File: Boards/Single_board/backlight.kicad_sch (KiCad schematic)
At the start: 38 parts

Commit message: some progress on the arduino boilerplate
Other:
- company: (none) -> Pablo Ortiz López, Evan MacDonald
- title: (none) -> Backlight for DSKY Keyboard
- moved on the sheet: D1, D10, D11, D12, D13, D14, D15, D16, D17, D18, D19, D2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

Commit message: Visual Schematic improvements
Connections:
- net PWMcom renamed PWMCom
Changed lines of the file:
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@@
 		)
 	)
-	(global_label "PWMcom"
-		(shape input)
+	(hierarchical_label "PWMCom"
+		(shape output)
 		(at 144.78 120.65 270)
 		(fields_autoplaced yes)
@@
 			(justify right)
 		)
-		(property "Intersheetrefs" "${INTERSHEET_REFS}"
-			(at 144.78 131.7389 90)
-			(effects
-				(font
-					(size 1.27 1.27)
-				)
-				(justify right)
-				(hide yes)
-			)
-		)
 	)

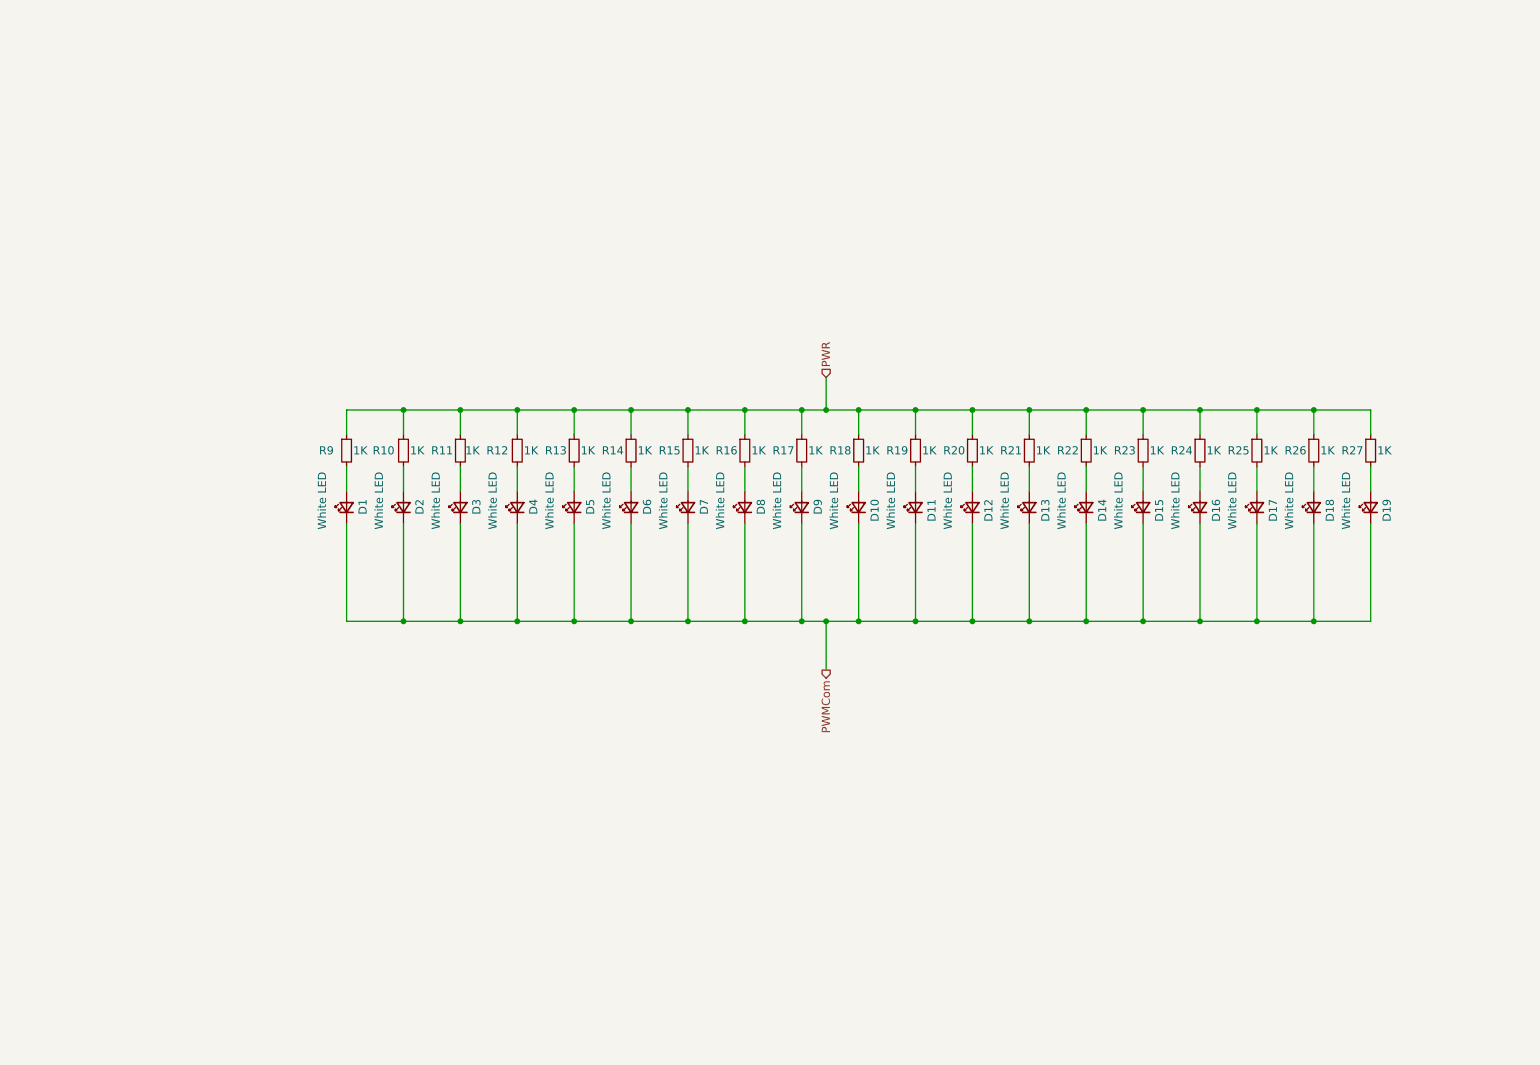
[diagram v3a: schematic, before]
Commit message: Start RGB LED + hotswap socket redesign of single board
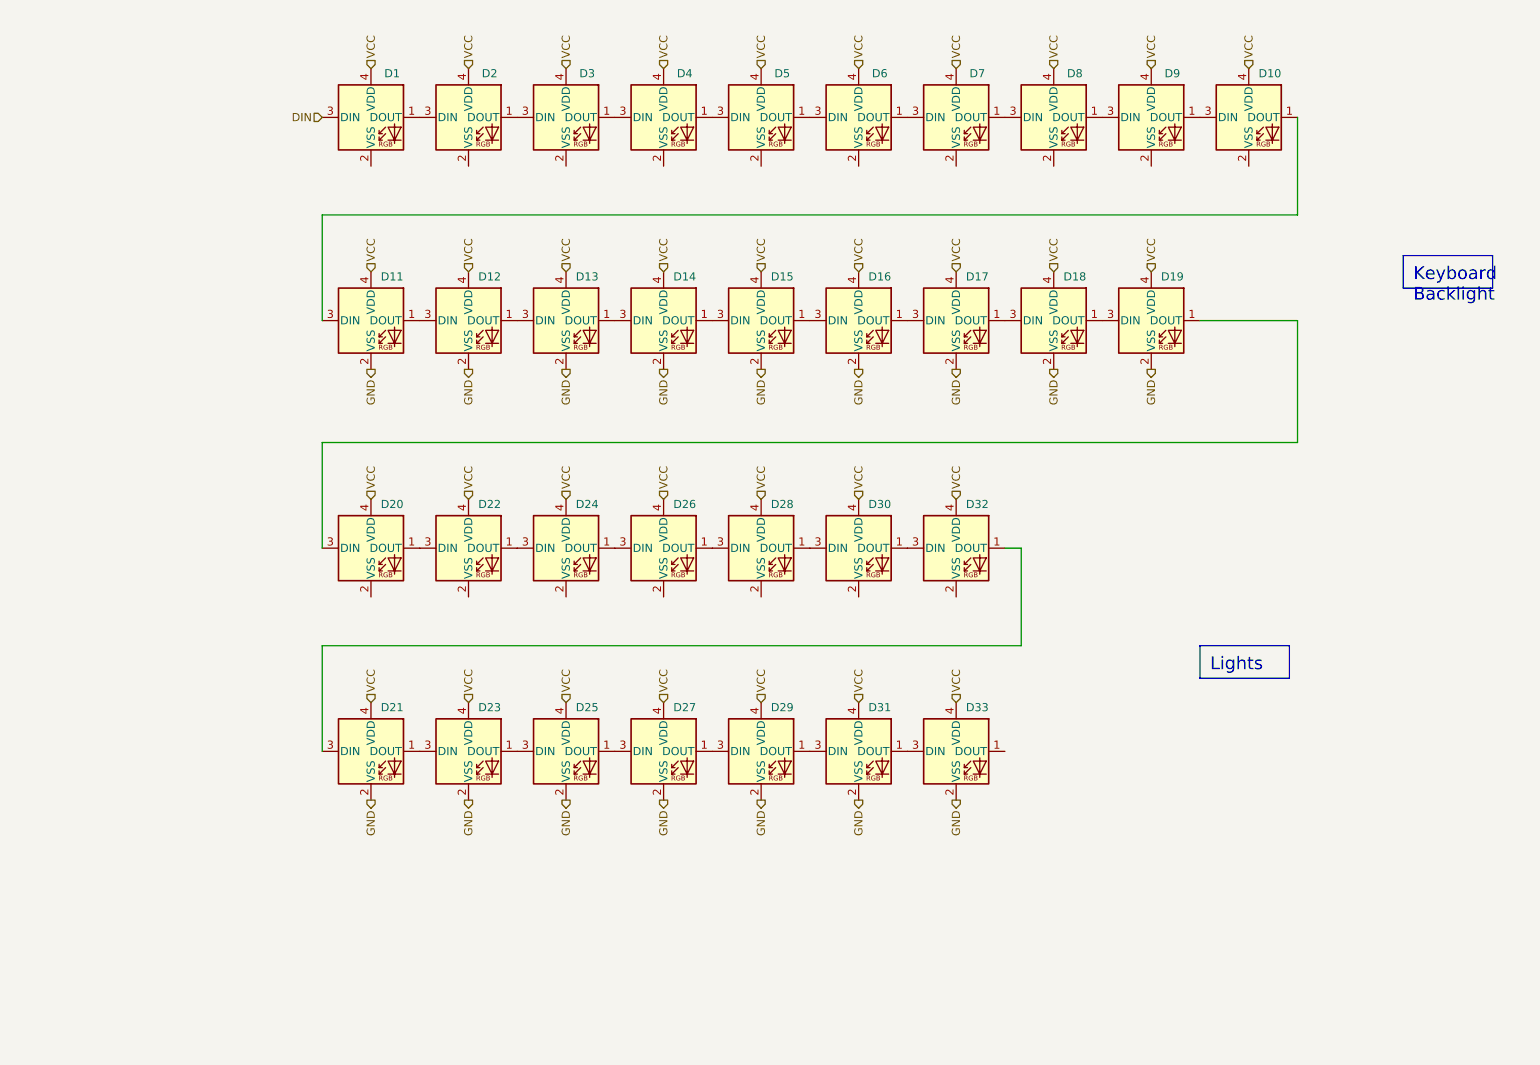
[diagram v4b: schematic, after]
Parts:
- removed D1, D10, D11, D12, D13, D14, D15, D16, D17, D18, D19, D2, D3, D4, D5, D6, D7, D8, D9: White LED, Switch_Misc:MX-LED-PolarityMarked, symbol Device:LED_Small
- removed R10, R11, R12, R13, R14, R15, R16, R17, R18, R19, R20, R21, R22, R23, R24, R25, R26, R27, R9: 1K, Resistor_SMD:R_1206_3216Metric, symbol Device:R_Small
- added D1, D10, D11, D12, D13, D14, D15, D16, D17, D18, D19, D2, D20, D21, D22, D23, D24, D25, D26, D27, D28, D29, D3, D30, D31, D32, D33, D4, D5, D6, D7, D8, D9: SK6812MINI, Project Libraries:SK6812-MINI-E, symbol LED:SK6812MINI
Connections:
- new net: D13.1 (DOUT), D14.3 (DIN)
- new net: D12.1 (DOUT), D13.3 (DIN)
- new net: D31.1 (DOUT), D33.3 (DIN)
- new net: D29.1 (DOUT), D31.3 (DIN)
- new net: D14.1 (DOUT), D15.3 (DIN)
- new net: D20.1 (DOUT), D22.3 (DIN)
- new net: D19.1 (DOUT), D20.3 (DIN)
- new net: D23.1 (DOUT), D25.3 (DIN)
- new net: D21.1 (DOUT), D23.3 (DIN)
- new net: D5.1 (DOUT), D6.3 (DIN)
- new net: D4.1 (DOUT), D5.3 (DIN)
- new net: D27.1 (DOUT), D29.3 (DIN)
- new net: D25.1 (DOUT), D27.3 (DIN)
- new net: D1.1 (DOUT), D2.3 (DIN)
- new net: D3.1 (DOUT), D4.3 (DIN)
- new net: D11.1 (DOUT), D12.3 (DIN)
- new net: D6.1 (DOUT), D7.3 (DIN)
- new net: D28.1 (DOUT), D30.3 (DIN)
- new net: D26.1 (DOUT), D28.3 (DIN)
- new net: D7.1 (DOUT), D8.3 (DIN)
- new net: D16.1 (DOUT), D17.3 (DIN)
- new net: D15.1 (DOUT), D16.3 (DIN)
- new net: D18.1 (DOUT), D19.3 (DIN)
- new net: D17.1 (DOUT), D18.3 (DIN)
- new net: D10.3 (DIN), D9.1 (DOUT)
- new net: D8.1 (DOUT), D9.3 (DIN)
- new net: D10.1 (DOUT), D11.3 (DIN)
- new net: D30.1 (DOUT), D32.3 (DIN)
- new net: D24.1 (DOUT), D26.3 (DIN)
- new net: D22.1 (DOUT), D24.3 (DIN)
- new net: D21.3 (DIN), D32.1 (DOUT)
- new net: D2.1 (DOUT), D3.3 (DIN)
- new net DIN: D1.3 (DIN)
- new net GND: D11.2 (VSS), D12.2 (VSS), D13.2 (VSS), D14.2 (VSS), D15.2 (VSS), D16.2 (VSS), D17.2 (VSS), D18.2 (VSS), D19.2 (VSS), D21.2 (VSS), D23.2 (VSS), D25.2 (VSS), D27.2 (VSS), D29.2 (VSS), D31.2 (VSS), D33.2 (VSS)
- new net VCC: D1.4 (VDD), D10.4 (VDD), D11.4 (VDD), D12.4 (VDD), D13.4 (VDD), D14.4 (VDD), D15.4 (VDD), D16.4 (VDD), D17.4 (VDD), D18.4 (VDD), D19.4 (VDD), D2.4 (VDD), D20.4 (VDD), D21.4 (VDD), D22.4 (VDD), D23.4 (VDD), D24.4 (VDD), D25.4 (VDD), D26.4 (VDD), D27.4 (VDD), D28.4 (VDD), D29.4 (VDD), D3.4 (VDD), D30.4 (VDD), D31.4 (VDD), D32.4 (VDD), D33.4 (VDD), D4.4 (VDD), D5.4 (VDD), D6.4 (VDD), D7.4 (VDD), D8.4 (VDD), D9.4 (VDD)

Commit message: Arrange and place components
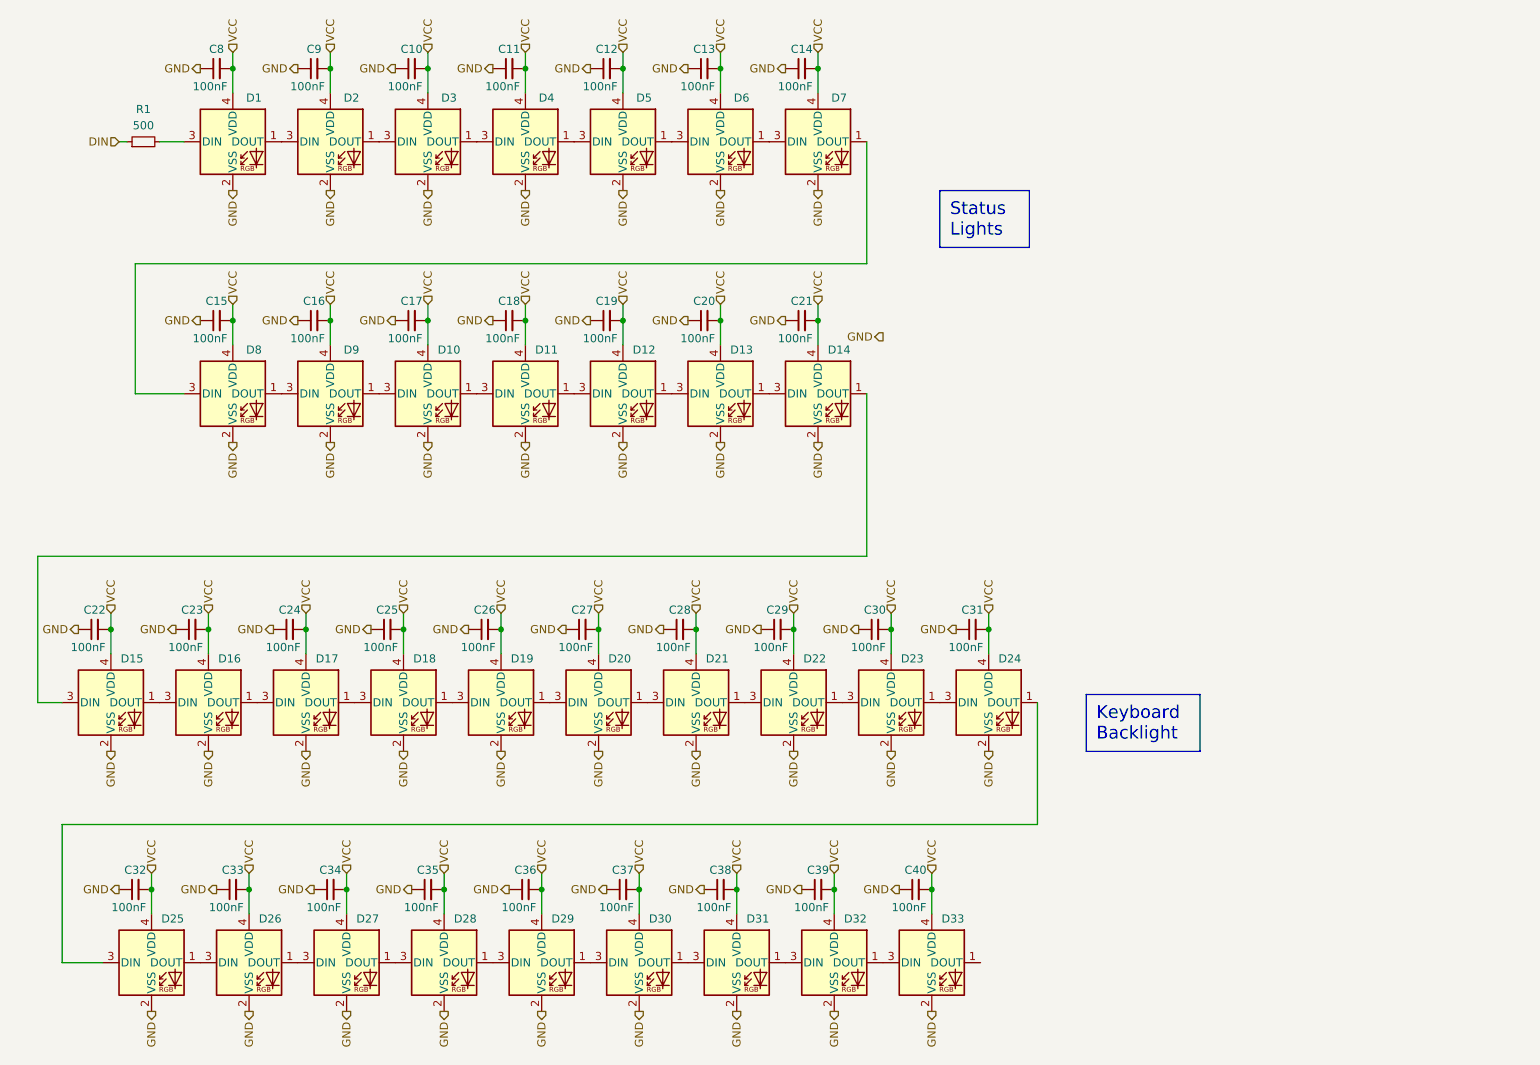
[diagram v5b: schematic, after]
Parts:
- added C10, C11, C12, C13, C14, C15, C16, C17, C18, C19, C20, C21, C22, C23, C24, C25, C26, C27, C28, C29, C30, C31, C32, C33, C34, C35, C36, C37, C38, C39, C40, C8, C9: 100nF, Capacitor_SMD:C_0805_2012Metric, symbol Device:C_Small
- added R1: 500, Resistor_SMD:R_1206_3216Metric, symbol Device:R_Small
- renumbered D22 to D21, D24 to D22, D26 to D23, D28 to D24, D30 to D25, D32 to D26, D21 to D27, D23 to D28, D25 to D29, D27 to D30, D29 to D31, D31 to D32
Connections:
- net DIN: now also R1.1; no longer D1.3 (DIN)
- net GND: now also D1.2 (VSS), D10.2 (VSS), D2.2 (VSS), D20.2 (VSS), D21.2 (VSS), D22.2 (VSS), D23.2 (VSS), D24.2 (VSS), D25.2 (VSS), D26.2 (VSS), D3.2 (VSS), D4.2 (VSS), D5.2 (VSS), D6.2 (VSS), D7.2 (VSS), D8.2 (VSS), D9.2 (VSS), C10.1, C11.1, C12.1, C13.1, C14.1, C15.1, C16.1, C17.1, C18.1, C19.1, C20.1, C21.1, C22.1, C23.1, C24.1, C25.1, C26.1, C27.1, C28.1, C29.1, C30.1, C31.1, C32.1, C33.1, C34.1, C35.1, C36.1, C37.1, C38.1, C39.1, C40.1, C8.1, C9.1
- net VCC: now also C10.2, C11.2, C12.2, C13.2, C14.2, C15.2, C16.2, C17.2, C18.2, C19.2, C20.2, C21.2, C22.2, C23.2, C24.2, C25.2, C26.2, C27.2, C28.2, C29.2, C30.2, C31.2, C32.2, C33.2, C34.2, C35.2, C36.2, C37.2, C38.2, C39.2, C40.2, C8.2, C9.2
- new net: D1.3 (DIN), R1.2
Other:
- moved on the sheet: D1, D10, D11, D12, D13, D14, D2, D20, D21, D22, D23, D24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

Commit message: Board and 3d models update
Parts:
- added C41: 100nF, Capacitor_SMD:C_0805_2012Metric, symbol Device:C_Small
- added D34: SK6812MINI, Project Libraries:SK6812-MINI-E, symbol LED:SK6812MINI
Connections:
- net GND: now also C41.1, D34.2 (VSS)
- net VCC: now also C41.2, D34.4 (VDD)
- net at D33.1 (DOUT): now also D34.3 (DIN)
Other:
- moved on the sheet: C22, C23, C24, C25, C26, C27, C28, C29, C30, C31, C32, C33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

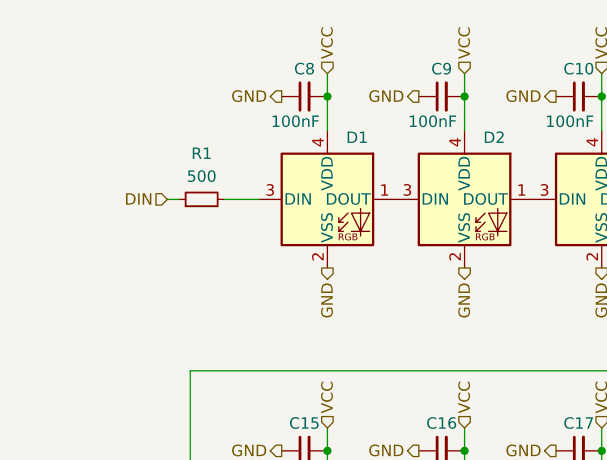
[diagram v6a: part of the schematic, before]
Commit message: Small routing improvements and prepare for JLC order
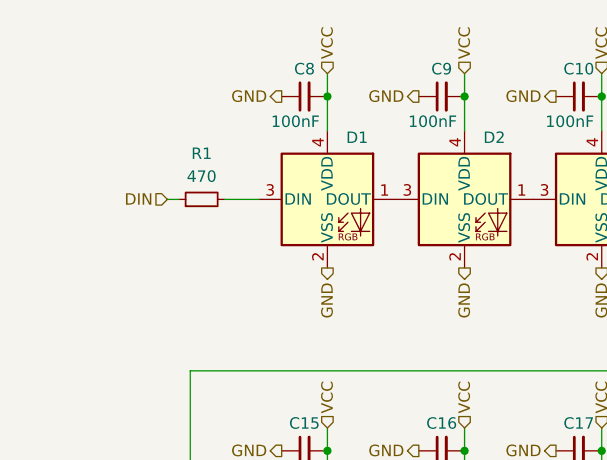
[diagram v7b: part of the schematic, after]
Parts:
- C10, C11, C12, C13, C14, C15, C16, C17, C18, C19, C20, C21, C22, C23, C24, C25, C26, C27, C28, C29, C30, C31, C32, C33, C34, C35, C36, C37, C38, C39, C40, C41, C8, C9: footprint Capacitor_SMD:C_0805_2012Metric -> Project Libraries:0805 100nF
- R1: value 500 -> 470; footprint Resistor_SMD:R_1206_3216Metric -> Resistor_SMD:R_0603_1608Metric
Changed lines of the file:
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@@
 			)
 		)
-		(property "Footprint" "Capacitor_SMD:C_0805_2012Metric"
+		(property "Footprint" "Project Libraries:0805 100nF"
 			(at 110.49 66.04 0)
 			(effects
@@
 			)
 		)
-		(property "Footprint" "Capacitor_SMD:C_0805_2012Metric"
+		(property "Footprint" "Project Libraries:0805 100nF"
 			(at 95.25 26.67 0)
 			(effects
@@
 			)
 		)
-		(property "Footprint" "Capacitor_SMD:C_0805_2012Metric"
+		(property "Footprint" "Project Libraries:0805 100nF"
 			(at 41.91 154.94 0)
 			(effects
@@
 			)
 		)
-		(property "Footprint" "Capacitor_SMD:C_0805_2012Metric"
+		(property "Footprint" "Project Libraries:0805 100nF"
 			(at 26.67 154.94 0)
 			(effects
@@
 			)
 		)
-		(property "Footprint" "Capacitor_SMD:C_0805_2012Metric"
+		(property "Footprint" "Project Libraries:0805 100nF"
 			(at 49.53 26.67 0)
 			(effects
@@
 			)
 		)
-		(property "Footprint" "Capacitor_SMD:C_0805_2012Metric"
+		(property "Footprint" "Project Libraries:0805 100nF"
 			(at 80.01 66.04 0)
 			(effects
@@
 			)
 		)
-		(property "Footprint" "Capacitor_SMD:C_0805_2012Metric"
+		(property "Footprint" "Project Libraries:0805 100nF"
 			(at 95.25 66.04 0)
 			(effects
@@
 			)
 		)
-		(property "Footprint" "Capacitor_SMD:C_0805_2012Metric"
+		(property "Footprint" "Project Libraries:0805 100nF"
 			(at 72.39 154.94 0)
 			(effects
@@
 			)
 		)
-		(property "Footprint" "Capacitor_SMD:C_0805_2012Metric"
+		(property "Footprint" "Project Libraries:0805 100nF"
 			(at 148.59 154.94 0)
 			(effects
@@
 			)
 		)
-		(property "Footprint" "Capacitor_SMD:C_0805_2012Metric"
+		(property "Footprint" "Project Libraries:0805 100nF"
 			(at 57.15 154.94 0)
 			(effects
@@
 			)
 		)
-		(property "Footprint" "Capacitor_SMD:C_0805_2012Metric"
+		(property "Footprint" "Project Libraries:0805 100nF"
 			(at 133.35 116.84 0)
 			(effects
@@
 			)
 		)
-		(property "Footprint" "Capacitor_SMD:C_0805_2012Metric"
+		(property "Footprint" "Project Libraries:0805 100nF"
 			(at 87.63 116.84 0)
 			(effects
@@
 			)
 		)
-		(property "Footprint" "Capacitor_SMD:C_0805_2012Metric"
+		(property "Footprint" "Project Libraries:0805 100nF"
 			(at 133.35 154.94 0)
 			(effects
@@
 			)
 		)
-		(property "Footprint" "Capacitor_SMD:C_0805_2012Metric"
+		(property "Footprint" "Project Libraries:0805 100nF"
 			(at 118.11 116.84 0)
 			(effects
@@
 			)
 		)
-		(property "Footprint" "Capacitor_SMD:C_0805_2012Metric"
+		(property "Footprint" "Project Libraries:0805 100nF"
 			(at 118.11 154.94 0)
 			(effects
@@
 			)
 		)
-		(property "Footprint" "Capacitor_SMD:C_0805_2012Metric"
+		(property "Footprint" "Project Libraries:0805 100nF"
 			(at 125.73 26.67 0)
 			(effects
@@
 			)
 		)
-		(property "Footprint" "Capacitor_SMD:C_0805_2012Metric"
+		(property "Footprint" "Project Libraries:0805 100nF"
 			(at 102.87 116.84 0)
 			(effects
@@
 			)
 		)
-		(property "Footprint" "Capacitor_SMD:C_0805_2012Metric"
+		(property "Footprint" "Project Libraries:0805 100nF"
 			(at 148.59 116.84 0)
 			(effects
@@
 			)
 		)
-		(property "Footprint" "Capacitor_SMD:C_0805_2012Metric"
+		(property "Footprint" "Project Libraries:0805 100nF"
 			(at 110.49 26.67 0)
 			(effects
@@
 			)
 		)
-		(property "Footprint" "Capacitor_SMD:C_0805_2012Metric"
+		(property "Footprint" "Project Libraries:0805 100nF"
 			(at 26.67 116.84 0)
 			(effects
@@
 			)
 		)
-		(property "Footprint" "Capacitor_SMD:C_0805_2012Metric"
+		(property "Footprint" "Project Libraries:0805 100nF"
 			(at 64.77 66.04 0)
 			(effects
@@
 			)
 		)
-		(property "Footprint" "Capacitor_SMD:C_0805_2012Metric"
+		(property "Footprint" "Project Libraries:0805 100nF"
 			(at 163.83 154.94 0)
 			(effects
@@
 			)
 		)
-		(property "Footprint" "Capacitor_SMD:C_0805_2012Metric"
+		(property "Footprint" "Project Libraries:0805 100nF"
 			(at 102.87 154.94 0)
 			(effects
@@
 			)
 		)
-		(property "Value" "500"
+		(property "Value" "470"
 			(at 38.1 35.56 90)
 			(effects
@@
 			)
 		)
-		(property "Footprint" "Resistor_SMD:R_1206_3216Metric"
+		(property "Footprint" "Resistor_SMD:R_0603_1608Metric"
 			(at 38.1 38.1 0)
 			(effects
@@
 			)
 		)
-		(property "Footprint" "Capacitor_SMD:C_0805_2012Metric"
+		(property "Footprint" "Project Libraries:0805 100nF"
 			(at 57.15 116.84 0)
 			(effects
@@
 			)
 		)
-		(property "Footprint" "Capacitor_SMD:C_0805_2012Metric"
+		(property "Footprint" "Project Libraries:0805 100nF"
 			(at 140.97 66.04 0)
 			(effects
@@
 			)
 		)
-		(property "Footprint" "Capacitor_SMD:C_0805_2012Metric"
+		(property "Footprint" "Project Libraries:0805 100nF"
 			(at 64.77 26.67 0)
 			(effects
@@
 			)
 		)
-		(property "Footprint" "Capacitor_SMD:C_0805_2012Metric"
+		(property "Footprint" "Project Libraries:0805 100nF"
 			(at 72.39 116.84 0)
 			(effects
@@
 			)
 		)
-		(property "Footprint" "Capacitor_SMD:C_0805_2012Metric"
+		(property "Footprint" "Project Libraries:0805 100nF"
 			(at 80.01 26.67 0)
 			(effects
@@
 			)
 		)
-		(property "Footprint" "Capacitor_SMD:C_0805_2012Metric"
+		(property "Footprint" "Project Libraries:0805 100nF"
 			(at 163.83 116.84 0)
 			(effects
@@
 			)
 		)
-		(property "Footprint" "Capacitor_SMD:C_0805_2012Metric"
+		(property "Footprint" "Project Libraries:0805 100nF"
 			(at 140.97 26.67 0)
 			(effects
@@
 			)
 		)
-		(property "Footprint" "Capacitor_SMD:C_0805_2012Metric"
+		(property "Footprint" "Project Libraries:0805 100nF"
 			(at 41.91 116.84 0)
 			(effects
@@
 			)
 		)
-		(property "Footprint" "Capacitor_SMD:C_0805_2012Metric"
+		(property "Footprint" "Project Libraries:0805 100nF"
 			(at 49.53 66.04 0)
 			(effects
@@
 			)
 		)
-		(property "Footprint" "Capacitor_SMD:C_0805_2012Metric"
+		(property "Footprint" "Project Libraries:0805 100nF"
 			(at 125.73 66.04 0)
 			(effects
@@
 			)
 		)
-		(property "Footprint" "Capacitor_SMD:C_0805_2012Metric"
+		(property "Footprint" "Project Libraries:0805 100nF"
 			(at 87.63 154.94 0)
 			(effects
